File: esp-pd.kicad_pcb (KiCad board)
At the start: 2 copper layers, 83 parts, among them J1 USB C Power, J2 USB C Data, J3 Power Out, J4 ESP PD Board pins, Q1 IRF7416, Q2 MMBT3904, SW1 Boot, SW2 Reset, SW3 Up, SW4 Down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

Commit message: preparing to route PCB x1
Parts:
- C21, C22, C23, C24, C25, C26, C27, D4, OLED1, R21, R22: moved to B.Cu
- moved U4 129.6 mm to (53.8, 153.9)
- moved D4 125.7 mm to (225.4, 137.5), turned to 180 degrees
- moved R22 122.8 mm to (224.1, 142.5), turned to 180 degrees
- moved Q1 122.5 mm to (142.5, 168.5)
- moved C21 121.0 mm to (209.3, 151.0), turned to 180 degrees
- moved C25 108.2 mm to (217.6, 139.5), turned to 180 degrees
- moved C27 106.7 mm to (215.1, 145.5), turned to 180 degrees
- moved R21 105.1 mm to (206.6, 144.5), turned to 180 degrees
- moved C26 102.6 mm to (212.6, 139.0), turned to 180 degrees
- moved U5 99.4 mm to (45.6, 127.8)
- moved C24 96.9 mm to (204.6, 139.0), turned to 180 degrees
- moved C14 96.9 mm to (46.6, 155.9)
- moved C22 96.1 mm to (197.6, 145.5), turned to 180 degrees
- moved R19 95.6 mm to (161.0, 169.4)
- moved C13 95.0 mm to (47.8, 151.9)
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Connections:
- U3 pad 10: unconnected-(U3-NC-Pad10) -> CC1
- U3 pad 6: unconnected-(U3-NC-Pad6) -> D+
- U3 pad 7: unconnected-(U3-NC-Pad7) -> D-
- U3 pad 9: unconnected-(U3-NC-Pad9) -> CC2
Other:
- copper layers 2 -> 4

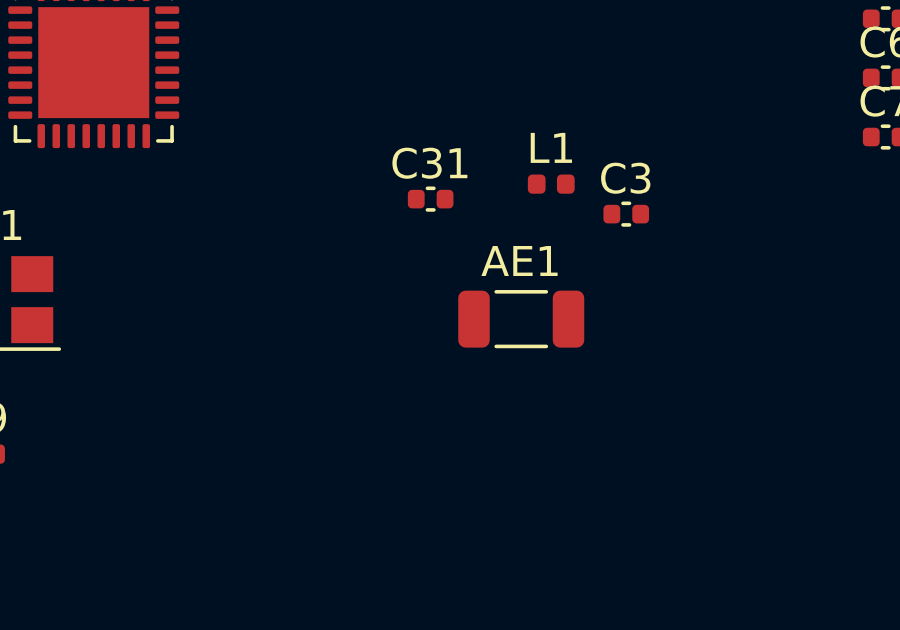
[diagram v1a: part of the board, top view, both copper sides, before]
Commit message: correct chip antenna footprint
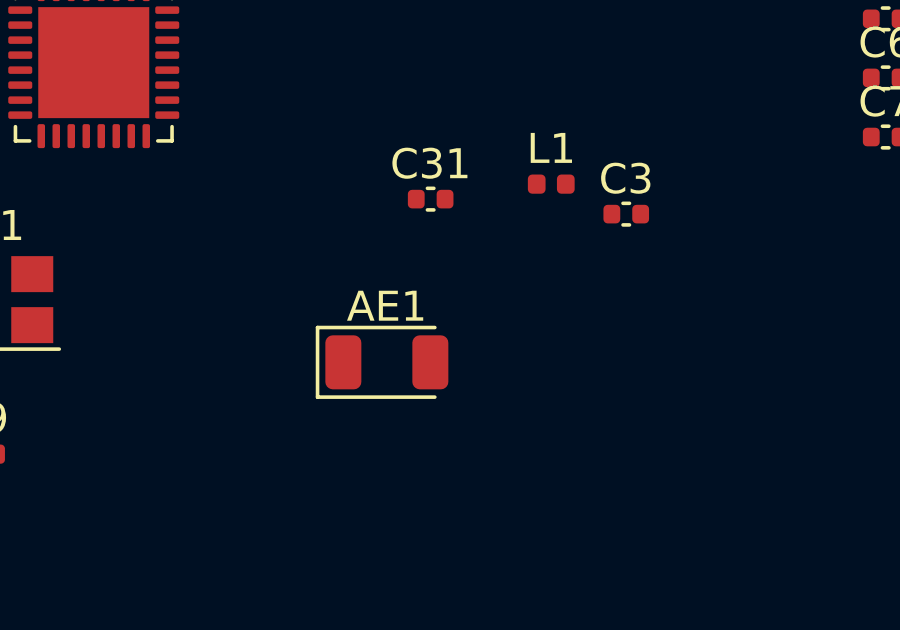
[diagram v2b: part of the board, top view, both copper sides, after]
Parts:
- AE1: footprint Inductor_SMD:L_1206_3216Metric -> RF_Antenna:Johanson_2450AT18x100
- moved AE1 4.71 mm to (136.0, 106.5)
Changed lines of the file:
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@@
 		(tags "DIP Switch SPST Slide 7.62mm 300mil")
 		(property "Reference" "SW5"
-			(at 3.81 -3.42 360)
+			(at 3.81 -3.42 0)
 			(layer "F.SilkS")
 			(effects
@@
 		)
 		(property "Value" "VBUS Switch"
-			(at 3.81 3.42 360)
+			(at 3.81 3.42 0)
 			(layer "F.Fab")
 			(effects
@@
 		)
 		(fp_text user "on"
-			(at 5.365 -1.4975 360)
+			(at 5.365 -1.4975 0)
 			(layer "F.Fab")
 			(effects
@@
 		)
 	)
-	(footprint "Inductor_SMD:L_1206_3216Metric"
+	(footprint "RF_Antenna:Johanson_2450AT18x100"
 		(layer "F.Cu")
-		(at 140.48 105.06)
-		(descr "Inductor SMD 1206 (3216 Metric), square (rectangular) end terminal, IPC_7351 nominal, (Body size source: IPC-SM-782 page 80, https://www.pcb-3d.com/wordpress/wp-content/uploads/ipc-sm-782a_amendment_1_and_2.pdf), generated with kicad-footprint-generator")
-		(tags "inductor")
+		(at 136 106.5)
+		(descr "Johanson 2450AT43F0100 SMD antenna 2400-2500Mhz, -0.5dBi, https://www.johansontechnology.com/datasheets/2450AT18A100/2450AT18A100.pdf")
+		(tags "antenna")
 		(property "Reference" "AE1"
-			(at 0 -1.9 0)
+			(at 0 -1.85 0)
 			(layer "F.SilkS")
 			(effects
@@
 		)
 		(property "Value" "Antenna_Chip"
-			(at 0.6175 1.66 0)
+			(at 0 1.85 0)
 			(layer "F.Fab")
 			(effects
@@
 			)
 		)
-		(property "Footprint" "Inductor_SMD:L_1206_3216Metric"
+		(property "Footprint" "RF_Antenna:Johanson_2450AT18x100"
 			(at 0 0 0)
 			(unlocked yes)
@@
 		(attr smd)
 		(fp_line
-			(start -0.835242 -0.91)
-			(end 0.835242 -0.91)
-			(stroke
-				(width 0.12)
-				(type solid)
-			)
-			(layer "F.SilkS")
-		)
-		(fp_line
-			(start -0.835242 0.91)
-			(end 0.835242 0.91)
-			(stroke
-				(width 0.12)
-				(type solid)
-			)
-			(layer "F.SilkS")
-		)
-		(fp_line
-			(start -2.35 -1.2)
-			(end 2.35 -1.2)
-			(stroke
-				(width 0.05)
-				(type solid)
-			)
-			(layer "F.CrtYd")
-		)
-		(fp_line
-			(start -2.35 1.2)
-			(end -2.35 -1.2)
-			(stroke
-				(width 0.05)
-				(type solid)
-			)
-			(layer "F.CrtYd")
-		)
-		(fp_line
-			(start 2.35 -1.2)
-			(end 2.35 1.2)
-			(stroke
-				(width 0.05)
-				(type solid)
-			)
-			(layer "F.CrtYd")
-		)
-		(fp_line
-			(start 2.35 1.2)
-			(end -2.35 1.2)
-			(stroke
-				(width 0.05)
-				(type solid)
-			)
-			(layer "F.CrtYd")
-		)
-		(fp_line
-			(start -1.6 -0.8)
+			(start -2.31 -1.16)
+			(end -2.31 1.16)
+			(stroke
+				(width 0.12)
+				(type solid)
+			)
+			(layer "F.SilkS")
+		)
+		(fp_line
+			(start -2.31 1.16)
+			(end 1.6 1.16)
+			(stroke
+				(width 0.12)
+				(type solid)
+			)
+			(layer "F.SilkS")
+		)
+		(fp_line
+			(start 1.6 -1.16)
+			(end -2.31 -1.16)
+			(stroke
+				(width 0.12)
+				(type solid)
+			)
+			(layer "F.SilkS")
+		)
+		(fp_line
+			(start -2.3 -1.15)
+			(end 2.3 -1.15)
+			(stroke
+				(width 0.05)
+				(type solid)
+			)
+			(layer "F.CrtYd")
+		)
+		(fp_line
+			(start -2.3 1.15)
+			(end -2.3 -1.15)
+			(stroke
+				(width 0.05)
+				(type solid)
+			)
+			(layer "F.CrtYd")
+		)
+		(fp_line
+			(start 2.3 -1.15)
+			(end 2.3 1.15)
+			(stroke
+				(width 0.05)
+				(type solid)
+			)
+			(layer "F.CrtYd")
+		)
+		(fp_line
+			(start 2.3 1.15)
+			(end -2.3 1.15)
+			(stroke
+				(width 0.05)
+				(type solid)
+			)
+			(layer "F.CrtYd")
+		)
+		(fp_line
+			(start -1.6 -0.4)
+			(end -1.6 0.8)
+			(stroke
+				(width 0.1)
+				(type solid)
+			)
+			(layer "F.Fab")
+		)
+		(fp_line
+			(start -1.6 0.8)
+			(end 1.6 0.8)
+			(stroke
+				(width 0.1)
+				(type solid)
+			)
+			(layer "F.Fab")
+		)
+		(fp_line
+			(start -1.2 -0.8)
+			(end -1.6 -0.4)
+			(stroke
+				(width 0.1)
+				(type solid)
+			)
+			(layer "F.Fab")
+		)
+		(fp_line
+			(start 1.6 -0.8)
+			(end -1.2 -0.8)
+			(stroke
+				(width 0.1)
+				(type solid)
+			)
+			(layer "F.Fab")
+		)
+		(fp_line
+			(start 1.6 0.8)
 			(end 1.6 -0.8)
-			(stroke
-				(width 0.1)
-				(type solid)
-			)
-			(layer "F.Fab")
-		)
-		(fp_line
-			(start -1.6 0.8)
-			(end -1.6 -0.8)
-			(stroke
-				(width 0.1)
-				(type solid)
-			)
-			(layer "F.Fab")
-		)
-		(fp_line
-			(start 1.6 -0.8)
-			(end 1.6 0.8)
-			(stroke
-				(width 0.1)
-				(type solid)
-			)
-			(layer "F.Fab")
-		)
-		(fp_line
-			(start 1.6 0.8)
-			(end -1.6 0.8)
 			(stroke
 				(width 0.1)
@@
 		)
 		(pad "1" smd roundrect
-			(at -1.575 0)
-			(size 1.05 1.9)
-			(layers "F.Cu" "F.Paste" "F.Mask")
-			(roundrect_rratio 0.238095)
+			(at -1.45 0)
+			(size 1.2 1.8)
+			(layers "F.Cu" "F.Paste" "F.Mask")
+			(roundrect_rratio 0.208333)
 			(net 2 "Net-(AE1-FEED)")
 			(pinfunction "FEED")
@@
 		)
 		(pad "2" smd roundrect
-			(at 1.575 0)
-			(size 1.05 1.9)
-			(layers "F.Cu" "F.Paste" "F.Mask")
-			(roundrect_rratio 0.238095)
+			(at 1.45 0)
+			(size 1.2 1.8)
+			(layers "F.Cu" "F.Paste" "F.Mask")
+			(roundrect_rratio 0.208333)
 			(net 1 "unconnected-(AE1-PCB_Trace-Pad2)")
 			(pinfunction "PCB_Trace")
 			(pintype "passive+no_connect")
 		)
-		(model "${KICAD8_3DMODEL_DIR}/Inductor_SMD.3dshapes/L_1206_3216Metric.wrl"
+		(model "${KICAD8_3DMODEL_DIR}/RF_Antenna.3dshapes/Johanson_2450AT18x100.wrl"
 			(offset
 				(xyz 0 0 0)

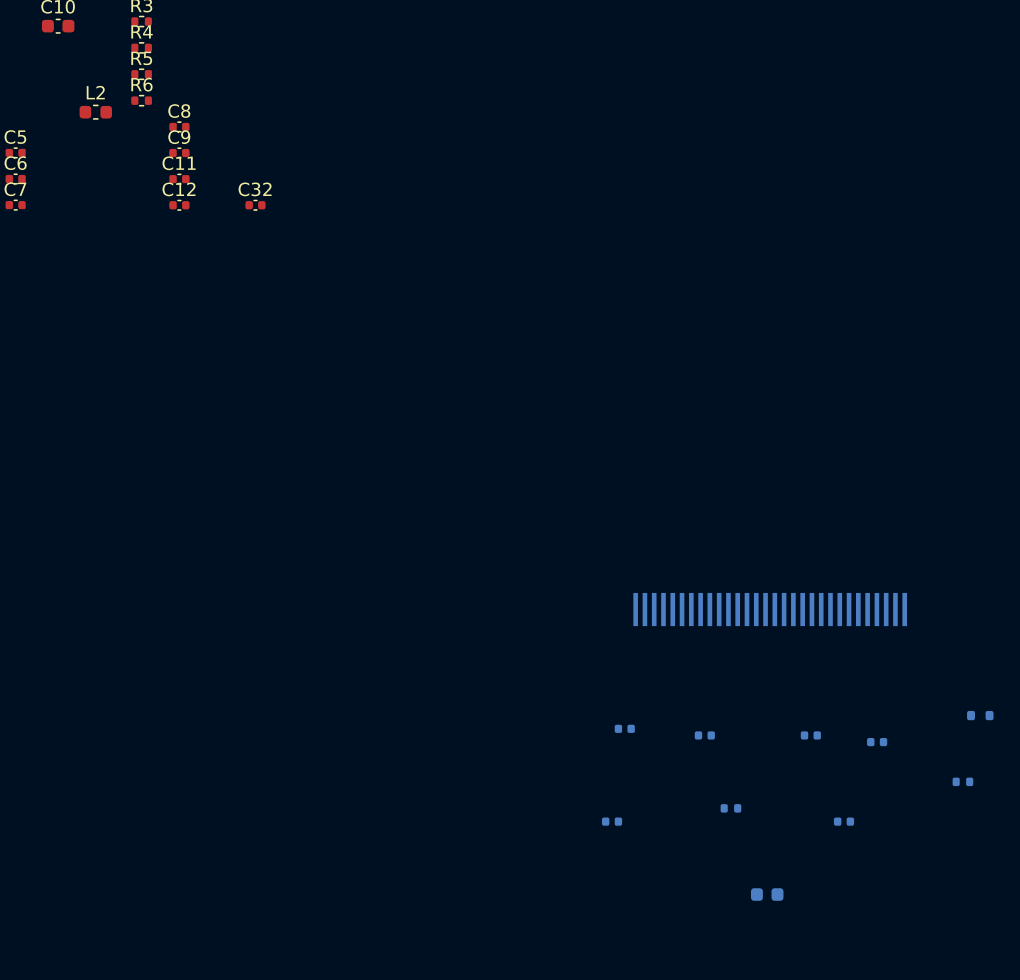
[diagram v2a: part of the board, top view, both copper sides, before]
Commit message: edited footprints
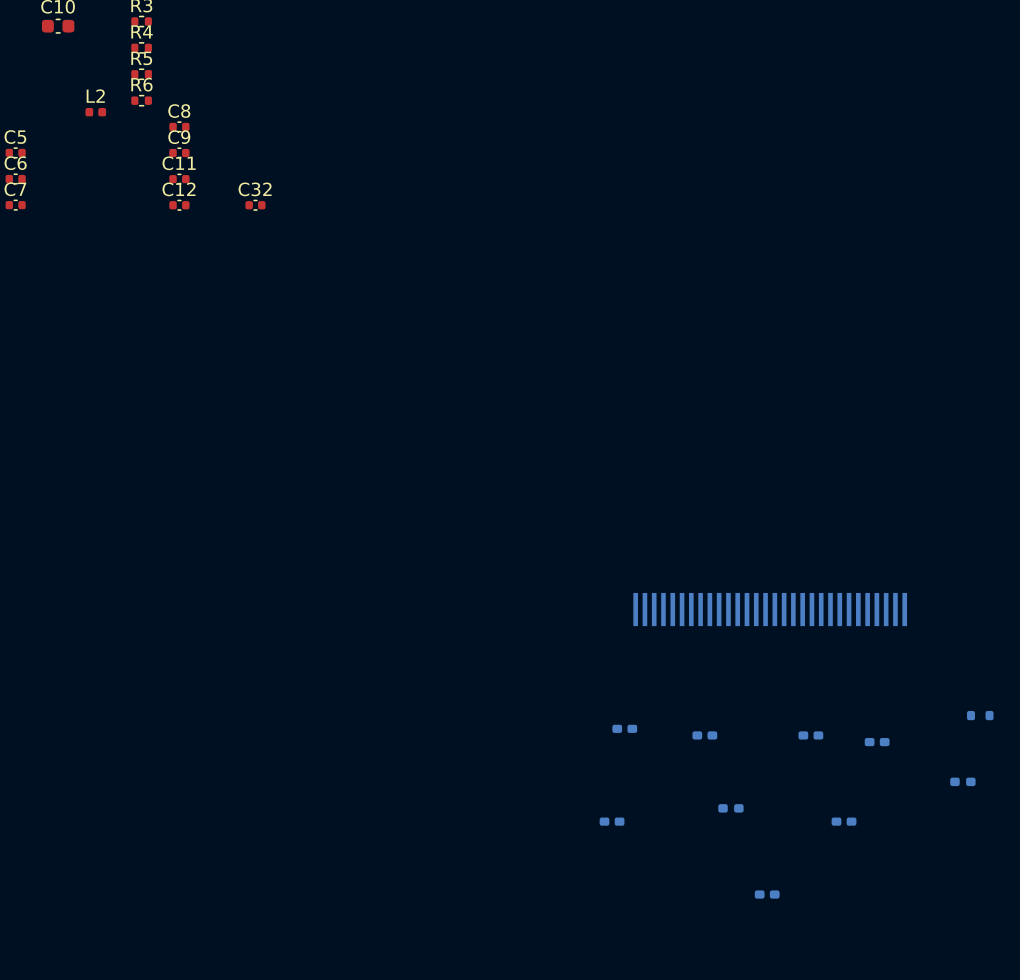
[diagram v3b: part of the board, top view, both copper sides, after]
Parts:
- C21: footprint Capacitor_SMD:C_0603_1608Metric -> Capacitor_SMD:C_0402_1005Metric_Pad0.74x0.62mm_HandSolder
- C22, C23, C24, C25, C26, C27: footprint Capacitor_SMD:C_0402_1005Metric -> Capacitor_SMD:C_0402_1005Metric_Pad0.74x0.62mm_HandSolder
- L2: value 2.2 nH -> 2.0 nH; footprint Inductor_SMD:L_0603_1608Metric -> Inductor_SMD:L_0402_1005Metric
- R21, R22: footprint Resistor_SMD:R_0402_1005Metric -> Resistor_SMD:R_0402_1005Metric_Pad0.72x0.64mm_HandSolder
